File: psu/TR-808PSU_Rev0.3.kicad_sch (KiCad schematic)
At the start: 73 parts, among them IC1 uA7805, IC2 TA7179P, P1 1, P10 10, P11 11, P12 12, P13 13, P14 14, P15 15, P16 16, P17 17, P18 18, P19 19, P2 2, P20 20, P21 21, P22 22, P3 3, P4 4, P5 5, P6 6, P7 7, P8 8, P9 9, Q1 2SB596, Q2 2SD880, SW1A SDG5P, SW1B SDG5P, T1 N-219D (220/240V)

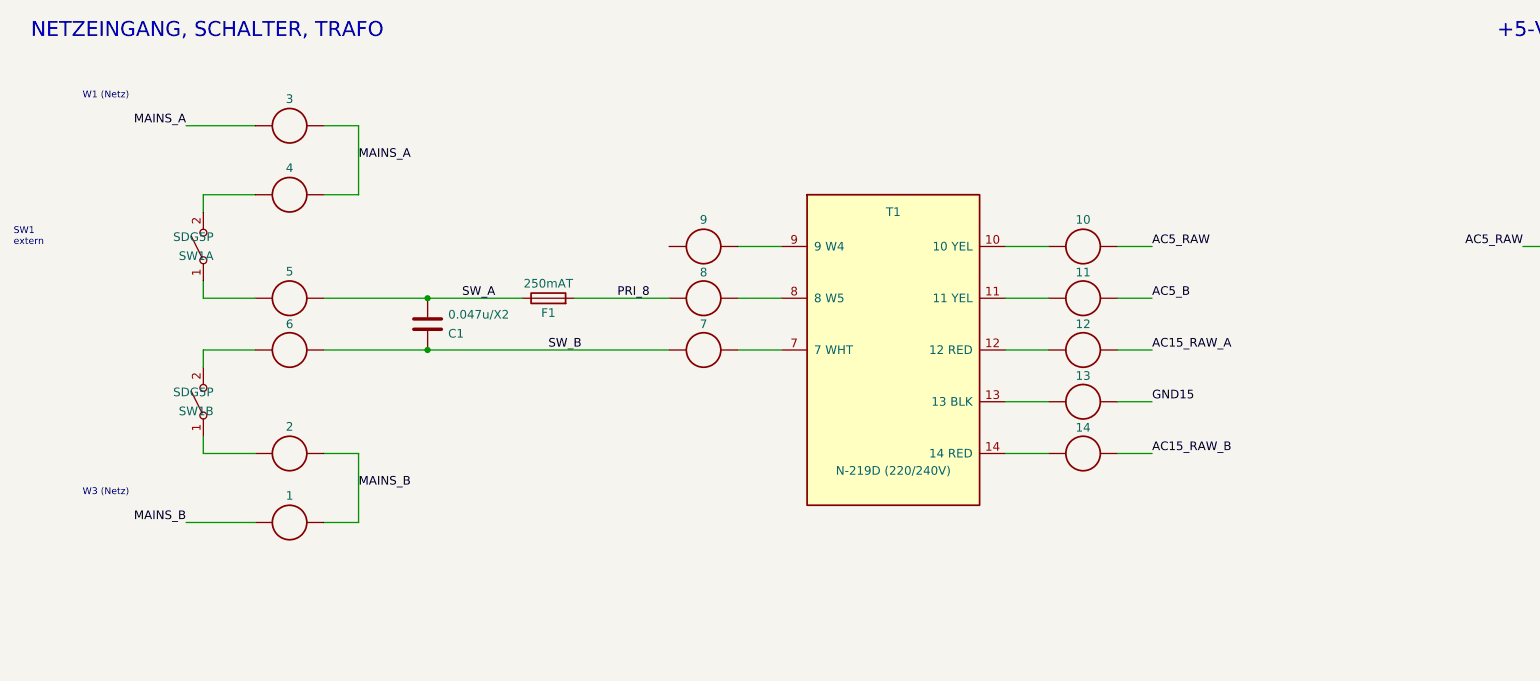
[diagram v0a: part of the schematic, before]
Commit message: Rev0.3: Schraubklemmen RM5 fuer die 230-V-Primaerseite (Klemmen 1-9)
Netz, Netzschalter und Trafo-Eingang (P1-P9) als vier Phoenix-MKDS-1,5-Bloecke X1-X4 statt Loetoesen.
Schaltplan, Platine, Siebdruck mit Klemmennummern, 3D, Gerber, Ausdruck neu. ERC 0, DRC 0 Fehler, Abgleich 0.

Co-Authored-By: Claude Sonnet 5.5 <noreply@anthropic.com>
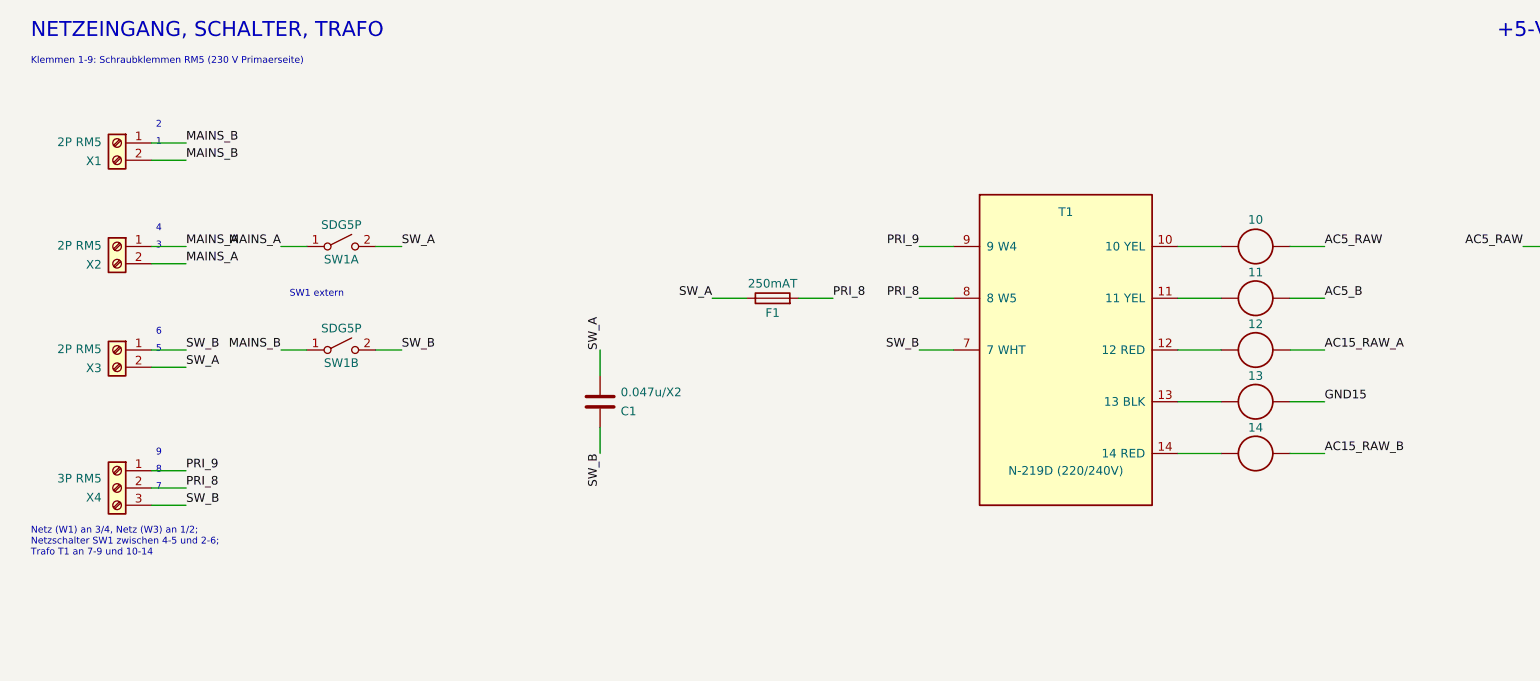
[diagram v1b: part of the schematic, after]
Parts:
- removed P1: 1, TR808PSU:Terminal_Pin, symbol TR808PSU:Terminal
- removed P2: 2, TR808PSU:Terminal_Pin, symbol TR808PSU:Terminal
- removed P3: 3, TR808PSU:Terminal_Pin, symbol TR808PSU:Terminal
- removed P4: 4, TR808PSU:Terminal_Pin, symbol TR808PSU:Terminal
- removed P5: 5, TR808PSU:Terminal_Pin, symbol TR808PSU:Terminal
- removed P6: 6, TR808PSU:Terminal_Pin, symbol TR808PSU:Terminal
- removed P7: 7, TR808PSU:Terminal_Pin, symbol TR808PSU:Terminal
- removed P8: 8, TR808PSU:Terminal_Pin, symbol TR808PSU:Terminal
- removed P9: 9, TR808PSU:Terminal_Pin, symbol TR808PSU:Terminal
- added X1, X2, X3: 2P RM5, TerminalBlock_Phoenix:TerminalBlock_Phoenix_MKDS-1,5-2_1x02_P5.00mm_Horizontal, symbol Connector:Screw_Terminal_01x02
- added X4: 3P RM5, TerminalBlock_Phoenix:TerminalBlock_Phoenix_MKDS-1,5-3_1x03_P5.00mm_Horizontal, symbol Connector:Screw_Terminal_01x03
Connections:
- net MAINS_A: now also SW1A.1 (A), X2.1 (Pin_1), X2.2 (Pin_2)
- net MAINS_B: now also SW1B.1 (A), X1.1 (Pin_1), X1.2 (Pin_2)
- net PRI_8: now also T1.8 (8 W5), X4.2 (Pin_2)
- net SW_A: now also SW1A.2 (B), X3.2 (Pin_2)
- net SW_B: now also SW1B.2 (B), T1.7 (7 WHT), X3.1 (Pin_1), X4.3 (Pin_3)
- net PRI_9: now reaches T1.9 (9 W4)
- net PRI_9: now also X4.1 (Pin_1)
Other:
- note added: "1"
- note added: "2"
- note added: "3"
- note added: "4"
- note added: "5"
- note added: "6"
- note added: "7"
- note added: "8"
- note added: "9"
- note added: "Klemmen 1-9: Schraubklemmen RM5 (230 V Primaerseite)"
- note added: "Netz (W1) an 3/4, Netz (W3) an 1/2; Netzschalter SW1 zwischen 4-5 und 2-6; Trafo T1 an 7-9 und 10-14"
- note removed: "W1 (Netz)"
- note removed: "W3 (Netz)"

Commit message: Docs and schematic in English, UNTESTED notice
Co-Authored-By: Claude Sonnet 5.5 <noreply@anthropic.com>
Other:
- note added: "+-15 V BRANCH (IC2 TA7179P, Q1, Q2)"
- note added: "+5 V BRANCH (IC1, RAM BACKUP)"
- note added: "Battery 3 x 1.5 V between 15 (-) and 16 (+)"
- note added: "MAINS INPUT, SWITCH, TRANSFORMER"
- note added: "MOUNTING: 4 board holes, 6 heat sink holes (246-101A), 3 screw holes for the regulators"
- note added: "Mains (W1) on 3/4, mains (W3) on 1/2; mains switch SW1 between 4-5 and 2-6; transformer T1 on 7-9 and 10-14"
- note added: "SW1 external"
- note added: "Terminals 1-9: RM5 screw terminals (230 V primary side)"
- note added: "UNTESTED - NOT MANUFACTURED, NOT MEASURED, NOT SAFETY-TESTED. MAINS VOLTAGE (230 V) CAN KILL. ROLAND TR-808 - POWER SUPPLY PS3116-054 (220/240 V), PCB 291-405A Redrawn from the service manual (15 June 1981): schematic sheet 13, component layout sheet 12, parts list sheet 10. Designators and terminal numbers 1-22 as in the original. Bridge rectifiers D1/D2: W04 (400 V, 2W04G on the unit); the manu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"
- note removed: "+-15-V-ZWEIG (IC2 TA7179P, Q1, Q2)"
- note removed: "+5-V-ZWEIG (IC1, RAM-PUFFER)"
- note removed: "BEFESTIGUNG: 4 Platinenbohrungen, 6 Kuehlkoerperbohrungen (246-101A), 3 Schraubenloecher der Regler"
- note removed: "Batterie 3 x 1,5 V zwischen 15 (-) und 16 (+)"
- note removed: "Klemmen 1-9: Schraubklemmen RM5 (230 V Primaerseite)"
- note removed: "NETZEINGANG, SCHALTER, TRAFO"
- note removed: "Netz (W1) an 3/4, Netz (W3) an 1/2; Netzschalter SW1 zwischen 4-5 und 2-6; Trafo T1 an 7-9 und 10-14"
- note removed: "ROLAND TR-808 - NETZTEIL PS3116-054 (220/240 V), PCB 291-405A Nachgezeichnet nach dem Service Manual (15.06.1981): Schaltbild Blatt 13, Bestueckungsplan Blatt 12, Stueckliste Blatt 10. Bauteilnummern und Anschluss- nummern 1-22 wie im Original. Brueckengleichrichter D1/D2: W04 (400 V, auf dem Geraet 2W04G); das Manual nennt W-02 (200 V), die W04 passt in dieselbe Bauform und ist ein zulaessiger E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"
- note removed: "SW1 extern"
- company: Nachzeichnung nach Roland TR-808 Service Notes, 15.06.1981 -> Redrawn from the Roland TR-808 service notes, 15 June 1981
- title: Roland TR-808 - Netzteil PS3116 (Nachbau 1:1) -> TR-808 PSU PS3116 rebuild - UNTESTED
